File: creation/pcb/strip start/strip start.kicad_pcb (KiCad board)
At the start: 2 copper layers, 15.5 x 15 mm, 5 parts, among them J1 Conn_01x03_Pin, J2 Conn_01x03_Pin, J3 Conn_01x01_Pin, J4 Conn_01x01_Pin, J5 Conn_01x02_Pin

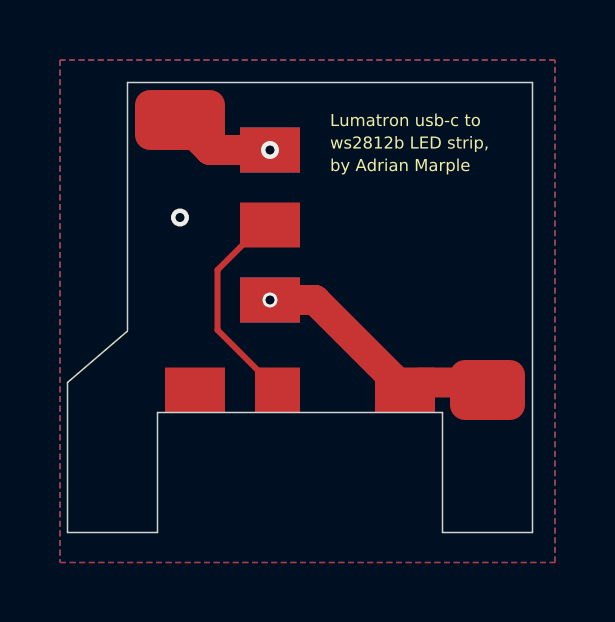
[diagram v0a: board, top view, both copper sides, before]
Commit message: New pcb for arduino box. Plus actually saved scad files and organized them a bit.
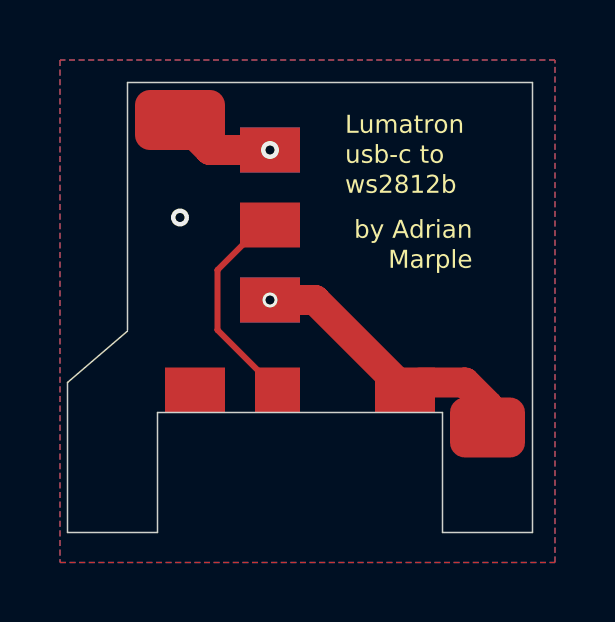
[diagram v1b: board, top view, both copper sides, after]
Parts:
- moved J4 1.25 mm to (41.2, 48.5)
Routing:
- net Net-(J1-Pin_3): track 7.60 -> 9.41 mm
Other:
- board text added: "Lumatron"
- board text added: "Marple"
- board text added: "by Adrian"
- board text added: "usb-c to"
- board text added: "ws2812b"
- board text removed: "Lumatron usb-c to"
- board text removed: "by Adrian Marple"
- board text removed: "ws2812b LED strip,"
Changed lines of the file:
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@@
 	(footprint "Connector_Wire:SolderWirePad_1x01_SMD_1x2mm"
 		(layer "F.Cu")
-		(at 41.25 47.25)
+		(at 41.25 48.5)
 		(descr "Wire Pad, Square, SMD Pad,  1mm x 2mm")
 		(tags "MeasurementPoint Square SMDPad 1mmx2mm ")
@@
 		(layer "Edge.Cuts")
 	)
-	(gr_text "by Adrian Marple"
-		(at 35.75 40 0)
+	(gr_text "by Adrian"
+		(at 40.5 42.25 0)
 		(layer "F.SilkS")
 		(effects
 			(font
-				(size 0.4 0.4)
+				(size 0.6 0.6)
 				(thickness 0.05)
 			)
-			(justify left bottom)
-		)
-	)
-	(gr_text "ws2812b LED strip,"
-		(at 35.75 39.25 0)
+			(justify right bottom)
+		)
+	)
+	(gr_text "usb-c to"
+		(at 36.25 39.75 0)
 		(layer "F.SilkS")
 		(effects
 			(font
-				(size 0.4 0.4)
+				(size 0.6 0.6)
 				(thickness 0.05)
 			)
@@
 		)
 	)
-	(gr_text "Lumatron usb-c to"
-		(at 35.75 38.5 0)
+	(gr_text "ws2812b"
+		(at 36.25 40.75 0)
 		(layer "F.SilkS")
 		(effects
 			(font
-				(size 0.4 0.4)
+				(size 0.6 0.6)
+				(thickness 0.05)
+			)
+			(justify left bottom)
+		)
+	)
+	(gr_text "Marple"
+		(at 40.5 43.25 0)
+		(layer "F.SilkS")
+		(effects
+			(font
+				(size 0.6 0.6)
+				(thickness 0.05)
+			)
+			(justify right bottom)
+		)
+	)
+	(gr_text "Lumatron"
+		(at 36.25 38.75 0)
+		(layer "F.SilkS")
+		(effects
+			(font
+				(size 0.6 0.6)
 				(thickness 0.05)
 			)
@@
 	)
 	(segment
+		(start 40.25 47)
+		(end 38.75 47)
+		(width 1)
+		(layer "F.Cu")
+		(net 2)
+	)
+	(segment
 		(start 35.25 44.25)
 		(end 38.25 47.25)
@@
 	)
 	(segment
-		(start 40.25 47)
-		(end 38.75 47)
+		(start 41 47.75)
+		(end 41 48.5)
 		(width 1)
 		(layer "F.Cu")
@@
 		(width 1)
 		(layer "F.Cu")
+		(net 2)
+	)
+	(segment
+		(start 40.25 47)
+		(end 41 47.75)
+		(width 1)
+		(layer "F.Cu")
